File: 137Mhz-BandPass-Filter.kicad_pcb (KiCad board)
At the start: 2 copper layers, 9 parts, among them J1 SMA, J2 SMA

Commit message: Final v0.1
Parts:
- removed J2: SMA, Connector_Coaxial:SMA_Molex_73251-1153_EdgeMount_Horizontal
- added G***: RiskeLogo, kicad-footprints-master:RiskeLogo, B.Cu at (116.0, 120.0)
- added J3: Conn_01x01, Connector_Wire:SolderWirePad_1x01_SMD_5x10mm, F.Cu at (167.2, 120.0)
- added MK1: Mounting_Hole_PAD, MountingHole:MountingHole_3.2mm_M3_Pad, F.Cu at (166.0, 114.0)
- added MK2: Mounting_Hole_PAD, MountingHole:MountingHole_3.2mm_M3_Pad, F.Cu at (102.0, 114.0)
- added MK3: Mounting_Hole_PAD, MountingHole:MountingHole_3.2mm_M3_Pad, F.Cu at (166.0, 126.0)
- added MK4: Mounting_Hole_PAD, MountingHole:MountingHole_3.2mm_M3_Pad, F.Cu at (102.0, 126.0)
- J1: value SMA -> Conn_01x01; footprint Connector_Coaxial:SMA_Molex_73251-1153_EdgeMount_Horizontal -> Connector_Wire:SolderWirePad_1x01_SMD_5x10mm
- moved J1 13.5 mm to (101.0, 120.0), turned to 90 degrees
- moved C5 9.20 mm to (151.2, 120.0)
- moved C1 9.20 mm to (116.1, 120.0)
- moved C2 9.20 mm to (128.0, 120.9)
- moved C3 9.20 mm to (134.0, 120.0)
- moved C4 9.20 mm to (140.0, 120.9)
- moved L1 9.20 mm to (122.5, 122.2)
- moved L2 9.20 mm to (145.5, 122.2)
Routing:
- net GND: track 102.8 -> 309.7 mm, vias 46 -> 130
- net Net-(C5-Pad1): track 5.81 -> 15.1 mm
- net Net-(C1-Pad2): track 11.6 -> 14.2 mm
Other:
- board outline added: 72 x 20 mm
- board text added: "137 MHz Band-pass filter"

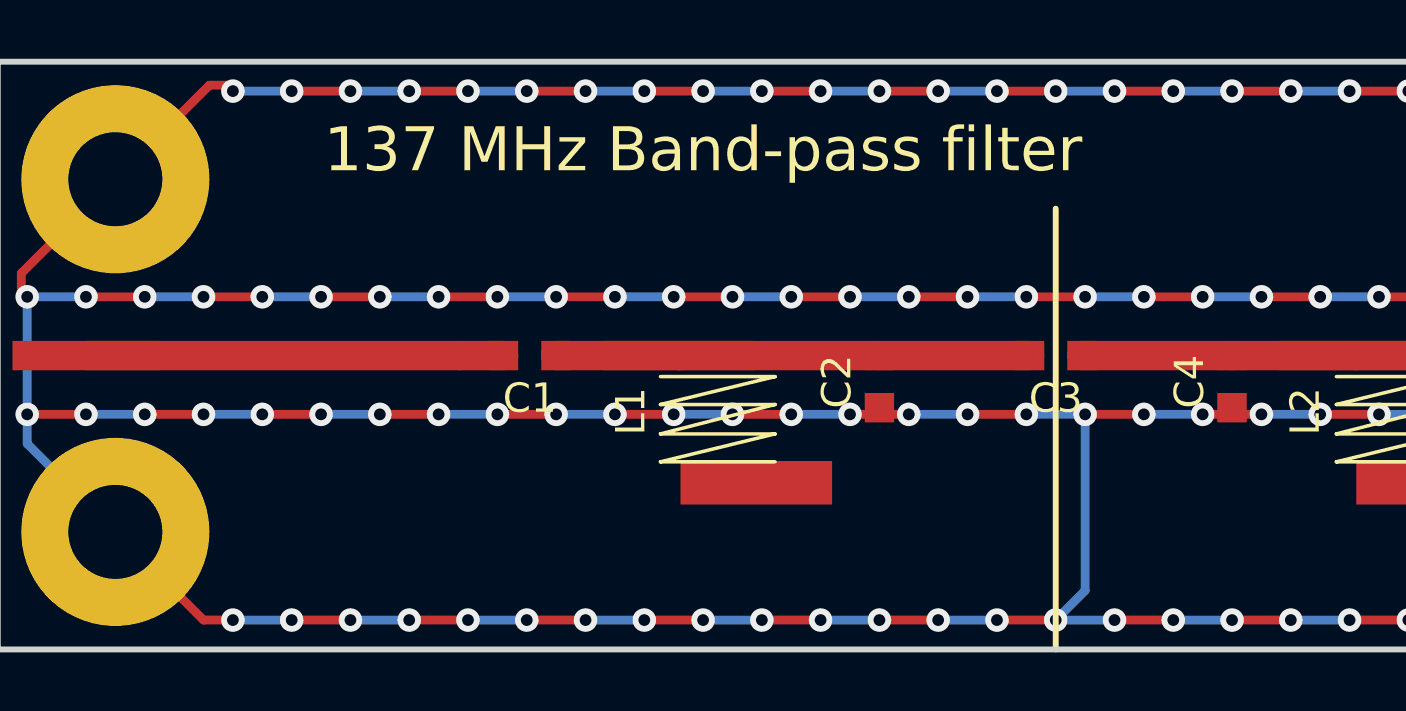
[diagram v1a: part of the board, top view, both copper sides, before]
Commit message: Added pads for shielding between coils
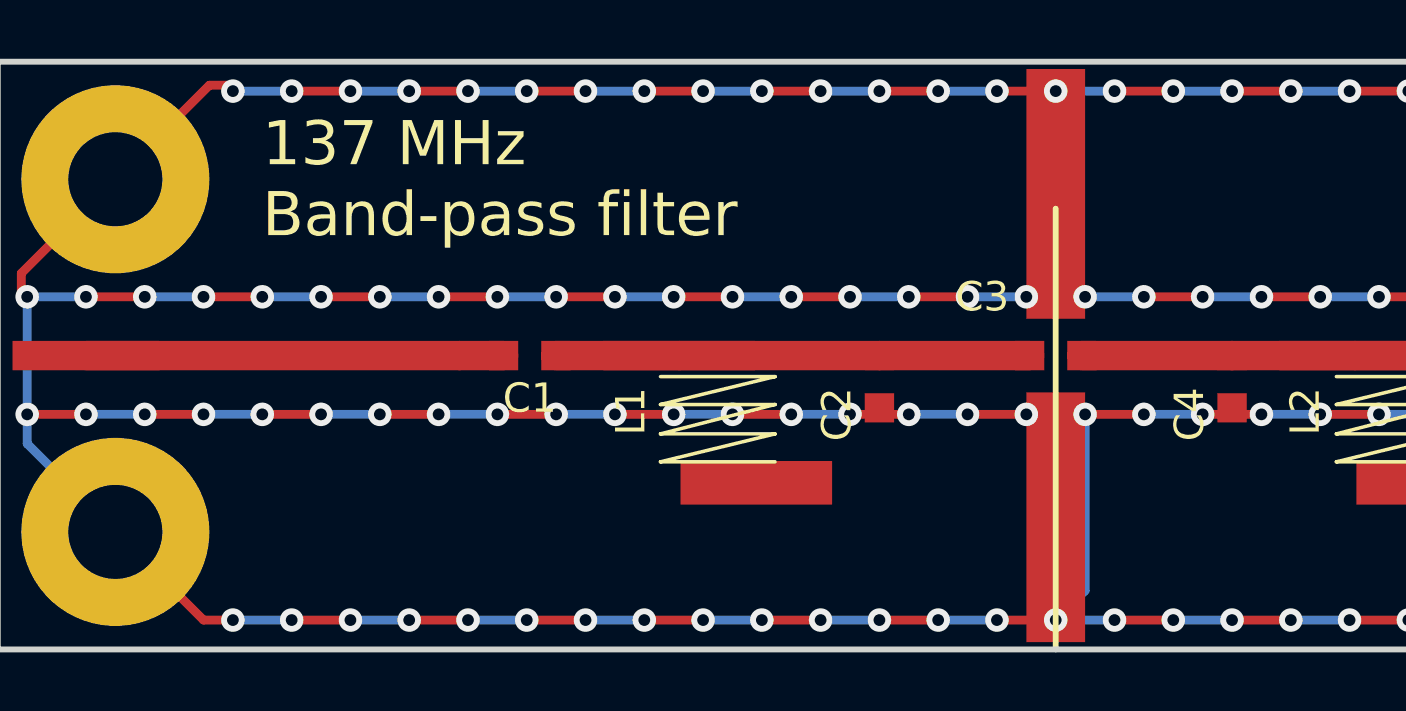
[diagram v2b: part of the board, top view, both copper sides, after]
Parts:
- added J2: Conn_01x01, Measurement_Points:Measurement_Point_Square-SMD-Pad_Big, F.Cu at (134.0, 125.5)
- added J4: Conn_01x01, Measurement_Points:Measurement_Point_Square-SMD-Pad_Big, F.Cu at (134.0, 114.5)
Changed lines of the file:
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@@
-(kicad_pcb (version 20171130) (host pcbnew "(5.0.2)-1")
+(kicad_pcb (version 20171130) (host pcbnew "(5.1.0-11-g23086decc)")
   (general
     (thickness 1.6)
@@
     (tracks 287)
     (zones 0)
-    (modules 14)
+    (modules 16)
     (nets 6)
   )
@@
     (zone_45_only no)
     (trace_min 0.2)
-    (segment_width 0.2)
-    (edge_width 0.15)
     (via_size 0.8)
     (via_drill 0.4)
@@
     (uvia_min_size 0.2)
     (uvia_min_drill 0.1)
+    (edge_width 0.15)
+    (segment_width 0.2)
     (pcb_text_width 0.3)
     (pcb_text_size 1.5 1.5)
@@
     (mod_text_size 1 1)
     (mod_text_width 0.15)
-    (pad_size 1 5)
+    (pad_size 2 8.5)
     (pad_drill 0)
     (pad_to_mask_clearance 0.051)
     (solder_mask_min_width 0.25)
     (aux_axis_origin 0 0)
-    (visible_elements 7FFFFFFF)
+    (visible_elements 7FFFEFFF)
     (pcbplotparams
       (layerselection 0x010fc_ffffffff)
@@
     (add_net "Net-(C5-Pad1)")
   )
+  (module Measurement_Points:Measurement_Point_Square-SMD-Pad_Big (layer F.Cu)
+    (at 134 125.5 180)
+    (descr "Mesurement Point, Square, SMD Pad,  3mm x 3mm,")
+    (tags "Mesurement Point Square SMD Pad 3x3mm")
+    (attr virtual)
+    (fp_text reference J2 (at 0 -2.667 180) (layer F.SilkS) hide
+      (effects (font (size 1 1) (thickness 0.15)))
+    )
+    (fp_text value Conn_01x01 (at 0 3.048 180) (layer F.Fab)
+      (effects (font (size 1 1) (thickness 0.15)))
+    )
+    (fp_line (start -1.75 -1.75) (end 1.75 -1.75) (layer F.CrtYd) (width 0.05))
+    (fp_line (start 1.75 -1.75) (end 1.75 1.75) (layer F.CrtYd) (width 0.05))
+    (fp_line (start 1.75 1.75) (end -1.75 1.75) (layer F.CrtYd) (width 0.05))
+    (fp_line (start -1.75 1.75) (end -1.75 -1.75) (layer F.CrtYd) (width 0.05))
+    (pad 1 smd rect (at 0 0 180) (size 2 8.5) (layers F.Cu F.Mask)
+      (net 1 GND))
+  )
+  (module Measurement_Points:Measurement_Point_Square-SMD-Pad_Big (layer F.Cu)
+    (at 134 114.5)
+    (descr "Mesurement Point, Square, SMD Pad,  3mm x 3mm,")
+    (tags "Mesurement Point Square SMD Pad 3x3mm")
+    (attr virtual)
+    (fp_text reference J4 (at 0 -3) (layer F.SilkS) hide
+      (effects (font (size 1 1) (thickness 0.15)))
+    )
+    (fp_text value Conn_01x01 (at 0 3) (layer F.Fab)
+      (effects (font (size 1 1) (thickness 0.15)))
+    )
+    (fp_line (start -1.75 -1.75) (end 1.75 -1.75) (layer F.CrtYd) (width 0.05))
+    (fp_line (start 1.75 -1.75) (end 1.75 1.75) (layer F.CrtYd) (width 0.05))
+    (fp_line (start 1.75 1.75) (end -1.75 1.75) (layer F.CrtYd) (width 0.05))
+    (fp_line (start -1.75 1.75) (end -1.75 -1.75) (layer F.CrtYd) (width 0.05))
+    (pad 1 smd rect (at 0 0) (size 2 8.5) (layers F.Cu F.Mask)
+      (net 1 GND))
+  )
   (module Capacitor_SMD:C_0603_1608Metric_Pad0.99x1.00mm_HandSolder (layer F.Cu)
     (at 134 120 180)
@@
     (tags "capacitor handsolder")
     (attr smd)
-    (fp_text reference C3 (at 0 -1.45 180) (layer F.SilkS)
+    (fp_text reference C3 (at 2.5 2 180) (layer F.SilkS)
       (effects (font (size 1 1) (thickness 0.15)))
     )
@@
     (tags "capacitor handsolder")
     (attr smd)
-    (fp_text reference C2 (at 0 -1.45 90) (layer F.SilkS)
+    (fp_text reference C2 (at -1.1125 -1.45 90) (layer F.SilkS)
       (effects (font (size 1 1) (thickness 0.15)))
     )
@@
     (tags "capacitor handsolder")
     (attr smd)
-    (fp_text reference C4 (at 0 -1.45 90) (layer F.SilkS)
+    (fp_text reference C4 (at -1.1125 -1.45 90) (layer F.SilkS)
       (effects (font (size 1 1) (thickness 0.15)))
     )
@@
     (effects (font (size 1.5 1.5) (thickness 0.3)) (justify mirror))
   )
-  (gr_text "137 MHz Band-pass filter" (at 122 113) (layer F.SilkS)
-    (effects (font (size 1.5 1.5) (thickness 0.3)))
+  (gr_text "137 MHz \nBand-pass filter" (at 107 114) (layer F.SilkS)
+    (effects (font (size 1.5 1.5) (thickness 0.3)) (justify left))
   )
   (dimension 20 (width 0.3) (layer F.SilkS)

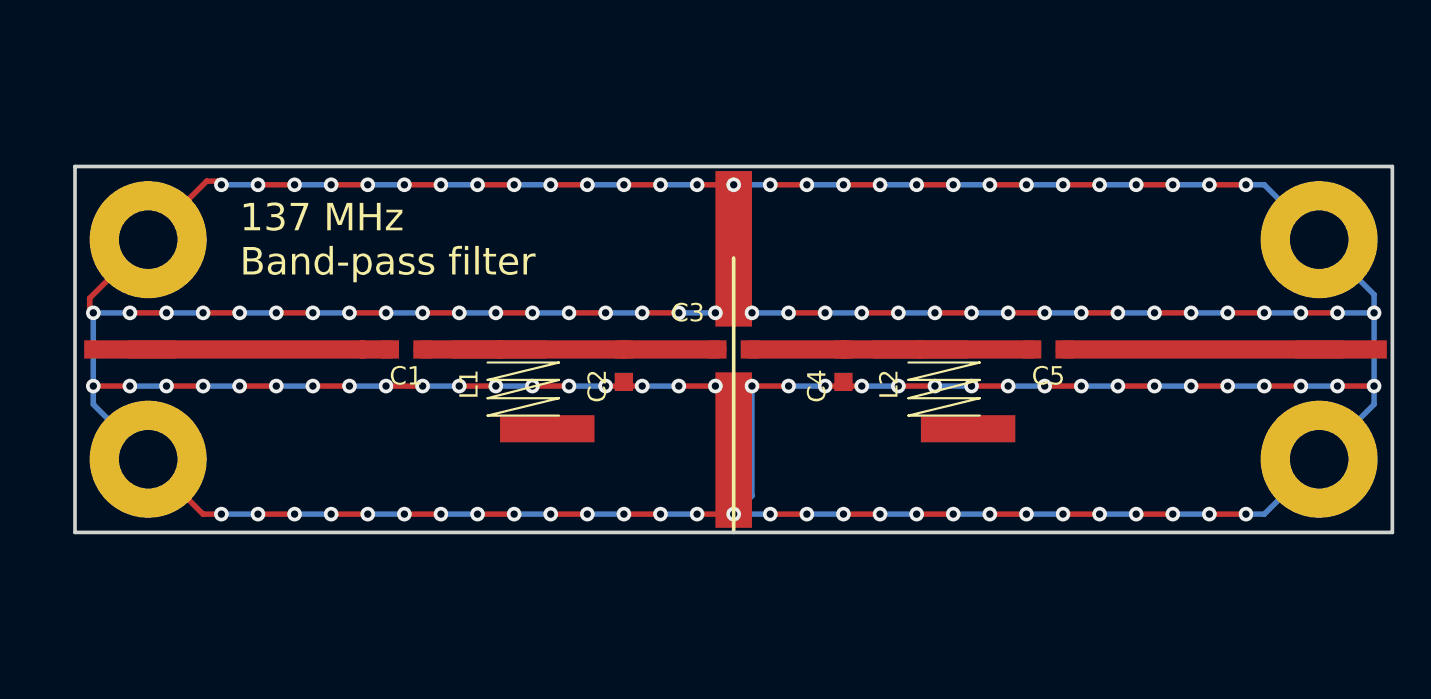
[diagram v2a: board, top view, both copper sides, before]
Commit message: Smaller PCB size
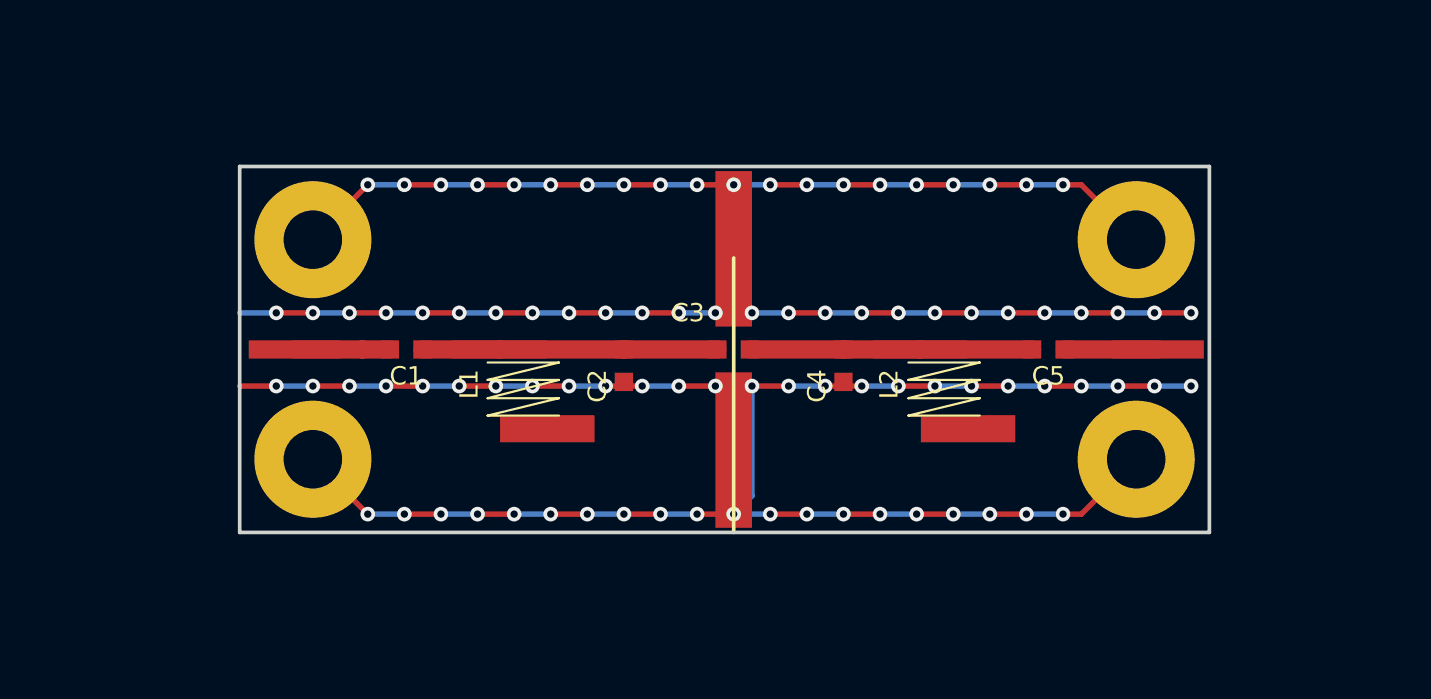
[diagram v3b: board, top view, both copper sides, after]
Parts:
- moved J3 10.0 mm to (157.2, 120.0)
- moved MK1 10.0 mm to (156.0, 114.0)
- moved MK3 10.0 mm to (156.0, 126.0)
- moved J1 9.00 mm to (110.0, 120.0)
- moved MK2 9.00 mm to (111.0, 114.0)
- moved MK4 9.00 mm to (111.0, 126.0)
- moved G*** 6.00 mm to (122.0, 120.0)
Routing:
- net GND: track 309.7 -> 206.4 mm, vias 130 -> 92
- net Net-(C5-Pad1): track 15.1 -> 5.11 mm
- net Net-(C1-Pad2): track 14.2 -> 5.21 mm
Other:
- board size 72 x 20 mm -> 53 x 20 mm
